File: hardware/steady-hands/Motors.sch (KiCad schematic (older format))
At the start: 10 parts, among them M1 Motor_DC, M2 Motor_DC, Q1 DMN2004WKQ, Q2 DMN2004WKQ

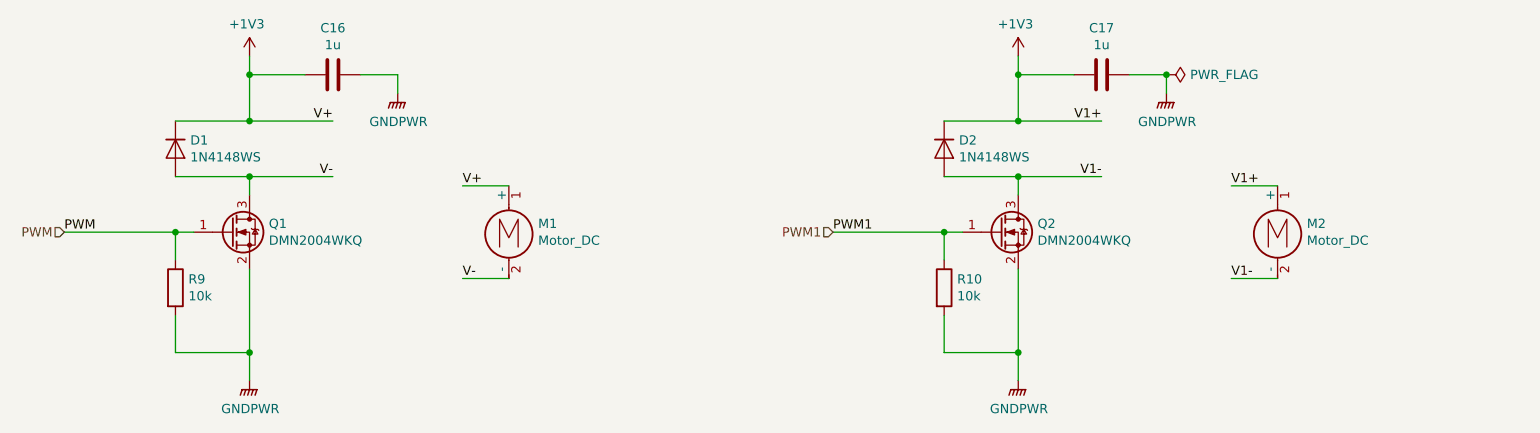
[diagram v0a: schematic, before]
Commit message: Edits PCB layout
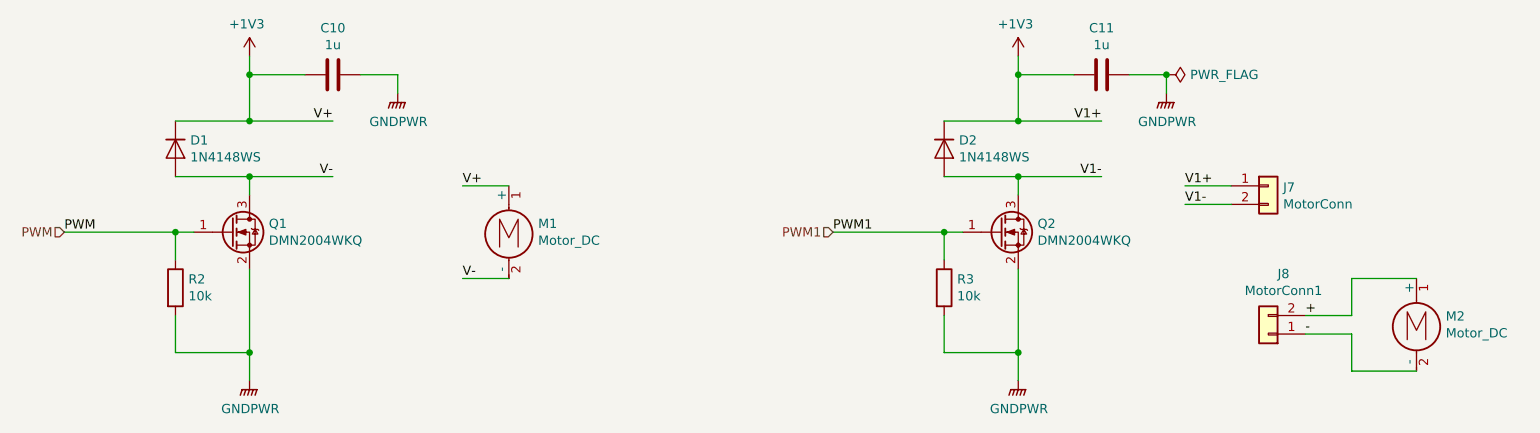
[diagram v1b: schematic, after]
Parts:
- added J7: MotorConn, Connector_PinHeader_1.27mm:PinHeader_1x02_P1.27mm_Vertical, symbol Connector_Generic:Conn_01x02
- added J8: MotorConn1, Connector_PinHeader_1.27mm:PinHeader_1x02_P1.27mm_Vertical, symbol Connector_Generic:Conn_01x02
- renumbered C16 to C10, C17 to C11, R9 to R2, R10 to R3
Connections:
- net +1V3: now also J7.1 (Pin_1); no longer M2.1 (+)
- net V1-: now also J7.2 (Pin_2); no longer M2.2 (-)
- new net +: J8.2 (Pin_2), M2.1 (+)
- new net -: J8.1 (Pin_1), M2.2 (-)
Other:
- moved on the sheet: M2
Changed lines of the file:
@@
 $EndDescr
 $Comp
-L Device:R R9
+L Device:R R2
 U 1 1 5EF9AE6E
 P 3050 4050
-F 0 "R9" H 3120 4096 50  0000 L CNN
+F 0 "R2" H 3120 4096 50  0000 L CNN
 F 1 "10k" H 3120 4005 50  0000 L CNN
 F 2 "Resistor_SMD:R_0402_1005Metric" V 2980 4050 50  0001 C CNN
@@
 $EndComp
 $Comp
-L Device:C C16
+L Device:C C10
 U 1 1 5EF9AE7A
 P 3900 2900
-F 0 "C16" V 3648 2900 50  0000 C CNN
+F 0 "C10" V 3648 2900 50  0000 C CNN
 F 1 "1u" V 3739 2900 50  0000 C CNN
 F 2 "Capacitor_SMD:C_0402_1005Metric" H 3938 2750 50  0001 C CNN
@@
 Connection ~ 3450 4400
 $Comp
-L power:GNDPWR #PWR0126
+L power:GNDPWR #PWR021
 U 1 1 5EF9AE97
 P 4250 3000
-F 0 "#PWR0126" H 4250 2800 50  0001 C CNN
+F 0 "#PWR021" H 4250 2800 50  0001 C CNN
 F 1 "GNDPWR" H 4254 2846 50  0000 C CNN
 F 2 "" H 4250 2950 50  0001 C CNN
@@
 $EndComp
 $Comp
-L power:GNDPWR #PWR0127
+L power:GNDPWR #PWR020
 U 1 1 5EF9AE9D
 P 3450 4550
-F 0 "#PWR0127" H 3450 4350 50  0001 C CNN
+F 0 "#PWR020" H 3450 4350 50  0001 C CNN
 F 1 "GNDPWR" H 3454 4396 50  0000 C CNN
 F 2 "" H 3450 4500 50  0001 C CNN
@@
 $EndComp
 $Comp
-L Device:R R10
+L Device:R R3
 U 1 1 5F074CD3
 P 7200 4050
-F 0 "R10" H 7270 4096 50  0000 L CNN
+F 0 "R3" H 7270 4096 50  0000 L CNN
 F 1 "10k" H 7270 4005 50  0000 L CNN
 F 2 "Resistor_SMD:R_0402_1005Metric" V 7130 4050 50  0001 C CNN
@@
 $EndComp
 $Comp
-L Device:C C17
+L Device:C C11
 U 1 1 5F074CDF
 P 8050 2900
-F 0 "C17" V 7798 2900 50  0000 C CNN
+F 0 "C11" V 7798 2900 50  0000 C CNN
 F 1 "1u" V 7889 2900 50  0000 C CNN
 F 2 "Capacitor_SMD:C_0402_1005Metric" H 8088 2750 50  0001 C CNN
@@
 Connection ~ 7600 4400
 $Comp
-L power:GNDPWR #PWR0128
+L power:GNDPWR #PWR024
 U 1 1 5F074CFA
 P 8400 3000
-F 0 "#PWR0128" H 8400 2800 50  0001 C CNN
+F 0 "#PWR024" H 8400 2800 50  0001 C CNN
 F 1 "GNDPWR" H 8404 2846 50  0000 C CNN
 F 2 "" H 8400 2950 50  0001 C CNN
@@
 $EndComp
 $Comp
-L power:GNDPWR #PWR0129
+L power:GNDPWR #PWR023
 U 1 1 5F074D00
 P 7600 4550
-F 0 "#PWR0129" H 7600 4350 50  0001 C CNN
+F 0 "#PWR023" H 7600 4350 50  0001 C CNN
 F 1 "GNDPWR" H 7604 4396 50  0000 C CNN
 F 2 "" H 7600 4500 50  0001 C CNN
@@
 Text Label 6600 3750 0    50   ~ 0
 PWM1
-Text Label 8750 3500 0    50   ~ 0
+Text Label 8500 3500 0    50   ~ 0
 V1+
-Text Label 8750 4000 0    50   ~ 0
+Text Label 8500 3600 0    50   ~ 0
 V1-
 Wire Wire Line
-	9000 3500 8750 3500
-Wire Wire Line
-	9000 4000 8750 4000
+	8750 3500 8500 3500
+Wire Wire Line
+	8750 3600 8500 3600
 Text HLabel 6600 3750 0    50   Input ~ 0
 PWM1
@@
 L Motor:Motor_DC M2
 U 1 1 5F074D16
-P 9000 3700
-F 0 "M2" H 9158 3696 50  0000 L CNN
-F 1 "Motor_DC" H 9158 3605 50  0000 L CNN
-F 2 "Sij_Motors:316040005" H 9000 3610 50  0001 C CNN
-F 3 "~" H 9000 3610 50  0001 C CNN
-	1    9000 3700
-	1    0    0    -1
-$EndComp
-$Comp
-L power:PWR_FLAG #FLG0107
+P 9750 4200
+F 0 "M2" H 9908 4196 50  0000 L CNN
+F 1 "Motor_DC" H 9908 4105 50  0000 L CNN
+F 2 "Sij_Motors:316040005" H 9750 4110 50  0001 C CNN
+F 3 "~" H 9750 4110 50  0001 C CNN
+	1    9750 4200
+	1    0    0    -1
+$EndComp
+$Comp
+L power:PWR_FLAG #FLG02
 U 1 1 5F25484B
 P 8400 2900
-F 0 "#FLG0107" H 8400 2975 50  0001 C CNN
+F 0 "#FLG02" H 8400 2975 50  0001 C CNN
 F 1 "PWR_FLAG" V 8400 3028 50  0000 L CNN
 F 2 "" H 8400 2900 50  0001 C CNN
@@
 Connection ~ 8400 2900
 $Comp
-L steady-hands:+1V3 #PWR0130
+L steady-hands:+1V3 #PWR019
 U 1 1 5F0DECEF
 P 3450 2850
-F 0 "#PWR0130" H 3550 2850 50  0001 C CNN
+F 0 "#PWR019" H 3550 2850 50  0001 C CNN
 F 1 "+1V3" H 3435 3073 50  0000 C CNN
 F 2 "" H 3450 2850 50  0001 C CNN
@@
 $EndComp
 $Comp
-L steady-hands:+1V3 #PWR0131
+L steady-hands:+1V3 #PWR022
 U 1 1 5F0DF498
 P 7600 2850
-F 0 "#PWR0131" H 7700 2850 50  0001 C CNN
+F 0 "#PWR022" H 7700 2850 50  0001 C CNN
 F 1 "+1V3" H 7585 3073 50  0000 C CNN
 F 2 "" H 7600 2850 50  0001 C CNN
@@
 	1    0    0    -1
 $EndComp
+$Comp
+L Connector_Generic:Conn_01x02 J7
+U 1 1 5F26A587
+P 8950 3500
+F 0 "J7" H 9030 3492 50  0000 L CNN
+F 1 "MotorConn" H 9030 3401 50  0000 L CNN
+F 2 "Connector_PinHeader_1.27mm:PinHeader_1x02_P1.27mm_Vertical" H 8950 3500 50  0001 C CNN
+F 3 "~" H 8950 3500 50  0001 C CNN
+	1    8950 3500
+	1    0    0    -1
+$EndComp
+Wire Wire Line
+	9150 4300 9400 4300
+$Comp
+L Connector_Generic:Conn_01x02 J8
+U 1 1 5F26EA67
+P 8950 4300
+F 0 "J8" H 8868 3975 50  0000 C CNN
+F 1 "MotorConn1" H 8868 4066 50  0000 C CNN
+F 2 "Connector_PinHeader_1.27mm:PinHeader_1x02_P1.27mm_Vertical" H 8950 4300 50  0001 C CNN
+F 3 "~" H 8950 4300 50  0001 C CNN
+	1    8950 4300
+	-1   0    0    1
+$EndComp
+Wire Wire Line
+	9150 4200 9400 4200
+Wire Wire Line
+	9750 4000 9400 4000
+Wire Wire Line
+	9400 4000 9400 4200
+Wire Wire Line
+	9400 4300 9400 4500
+Wire Wire Line
+	9400 4500 9750 4500
+Text Label 9150 4200 0    50   ~ 0
++
+Text Label 9150 4300 0    50   ~ 0
+-
 $EndSCHEMATC
